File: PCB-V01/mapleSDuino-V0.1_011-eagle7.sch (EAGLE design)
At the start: 12 parts, among them IC2 LAN-USR-ES1

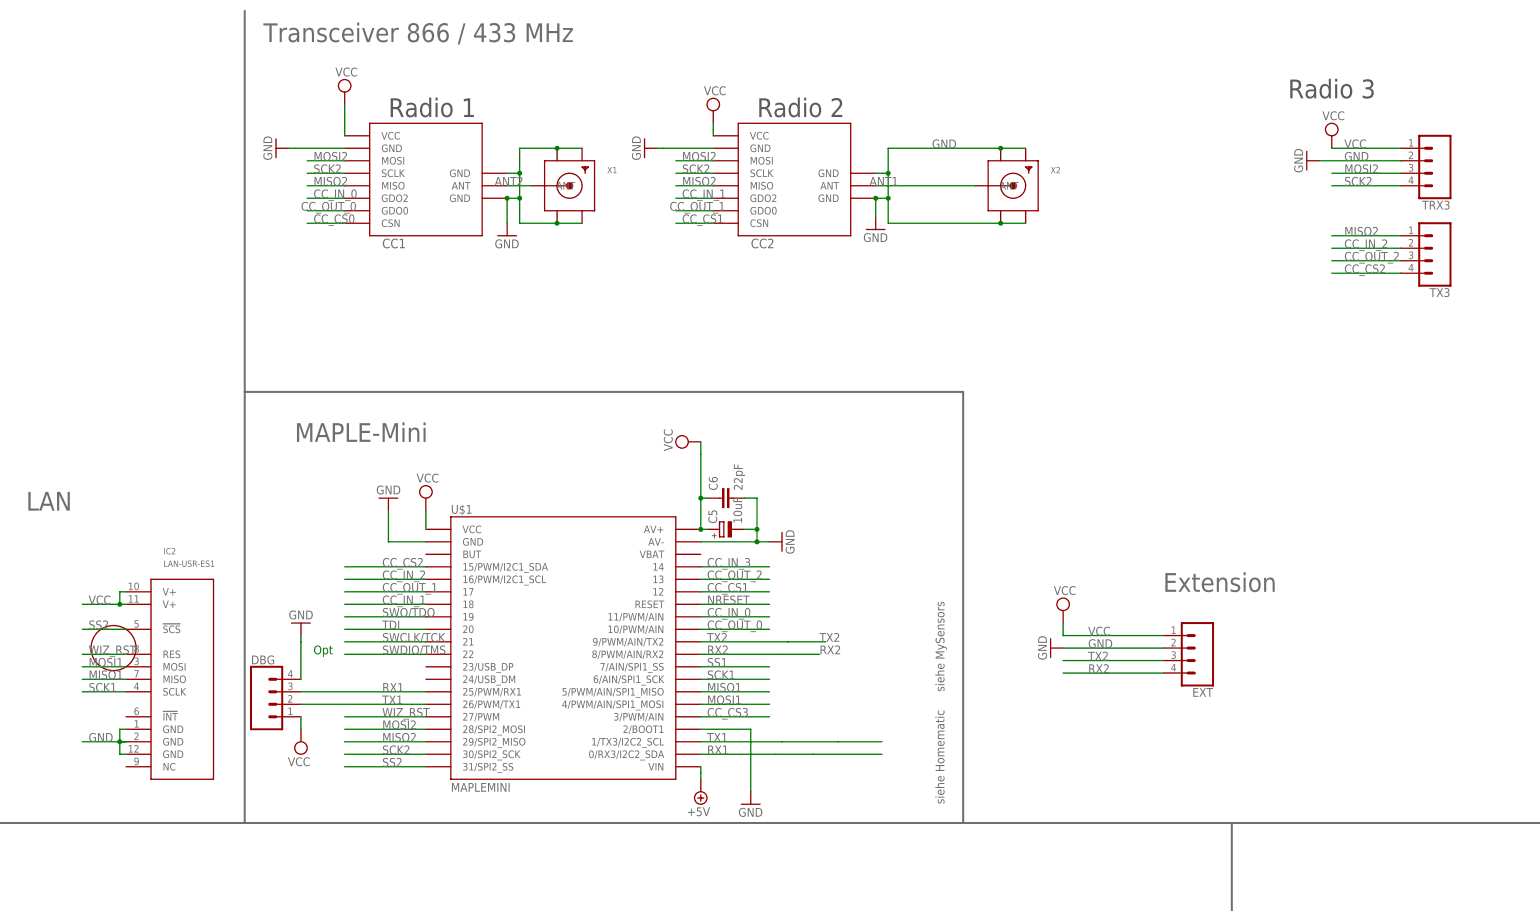
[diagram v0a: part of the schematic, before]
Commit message: Update
SPI + TRX Pins, Shielding, 5V Pin
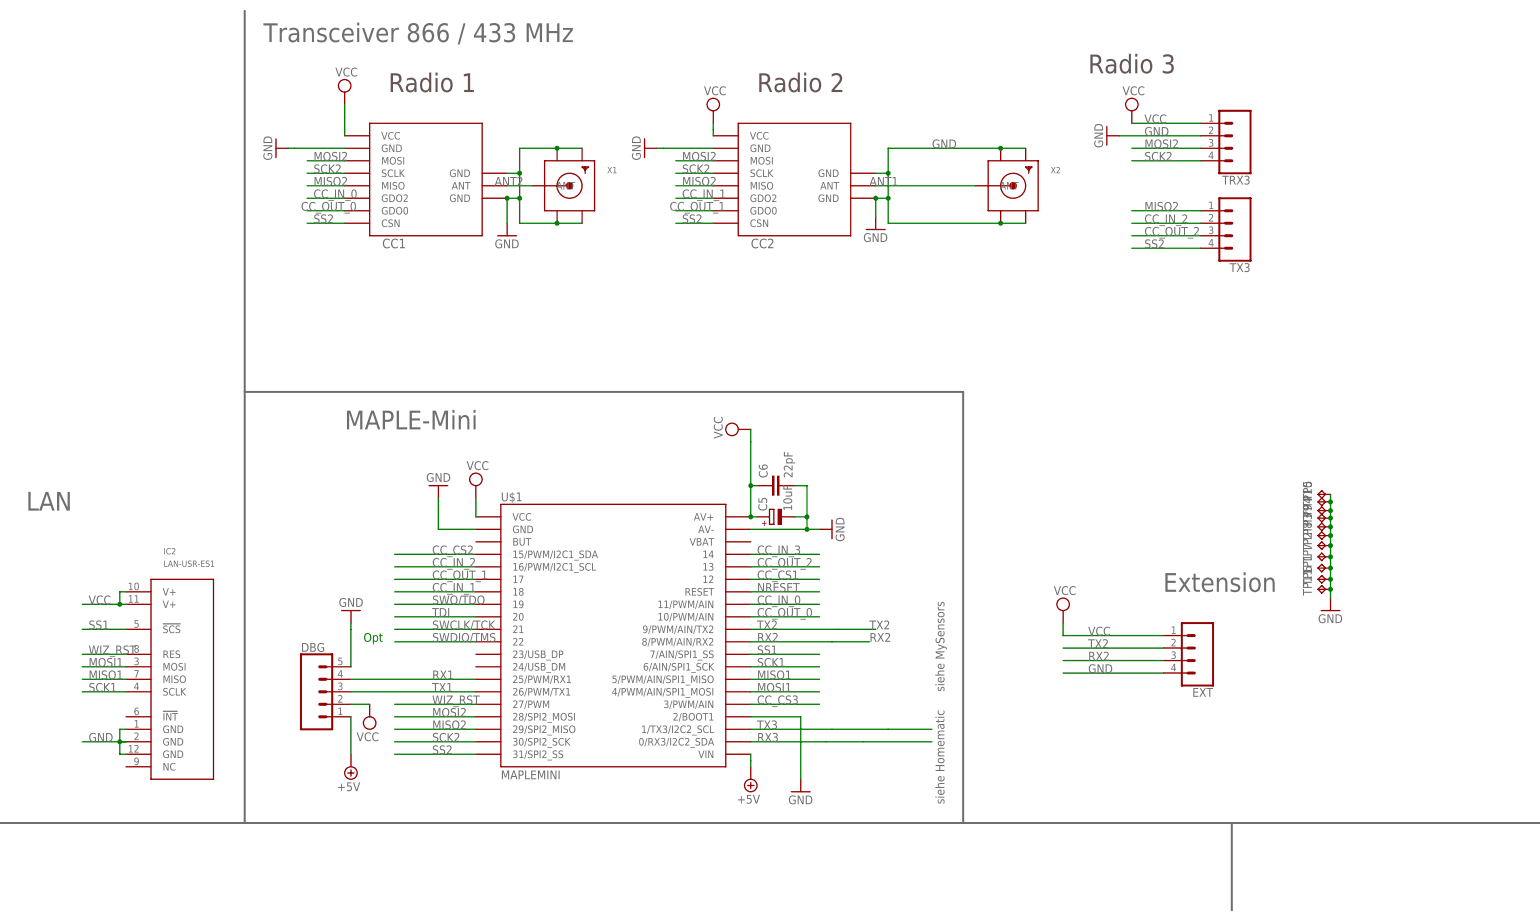
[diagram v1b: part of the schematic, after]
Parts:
- added TP1, TP10, TP11, TP2, TP3, TP4, TP5, TP6, TP7, TP8, TP9: TPTP06SQ, testpad:TPTP06SQ
- DBG: device SparkFun-Connectors:CONN_04LOCK -> SparkFun-Connectors:CONN_05LOCK
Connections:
- removed net CC_CS0: CC1.CSN
- new net RX3: U$1.0/RX3/I2C2_SDA
- new net TX3: U$1.1/TX3/I2C2_SCL
- net +5V: now also DBG.1
- net CC_CS1: no longer CC2.CSN
- net CC_CS2: no longer TX3.4
- net GND: now also DBG.5, EXT.4, TP1.TP, TP10.TP, TP11.TP, TP2.TP, TP3.TP, TP4.TP, TP5.TP, TP6.TP, TP7.TP, TP8.TP, TP9.TP; no longer DBG.4, EXT.2
- net RX1: now also DBG.4; no longer DBG.3, U$1.0/RX3/I2C2_SDA
- net RX2: now also EXT.3; no longer EXT.4
- net SS1: now also IC2.!SCS!
- net SS2: now also CC1.CSN, CC2.CSN, TX3.4; no longer IC2.!SCS!
- net TX1: now also DBG.3; no longer DBG.2, U$1.1/TX3/I2C2_SCL
- net TX2: now also EXT.2; no longer EXT.3
- net VCC: now also DBG.2; no longer DBG.1
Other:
- moved on the sheet: C5, C6, TRX3, TX3, U$1
